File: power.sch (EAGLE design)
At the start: 19 parts, among them Q1 12V/6A, U1 LTC4412HV, X1 5566-4-RIGHTANGLE, X3 RASPI_BOARD_B+#_H

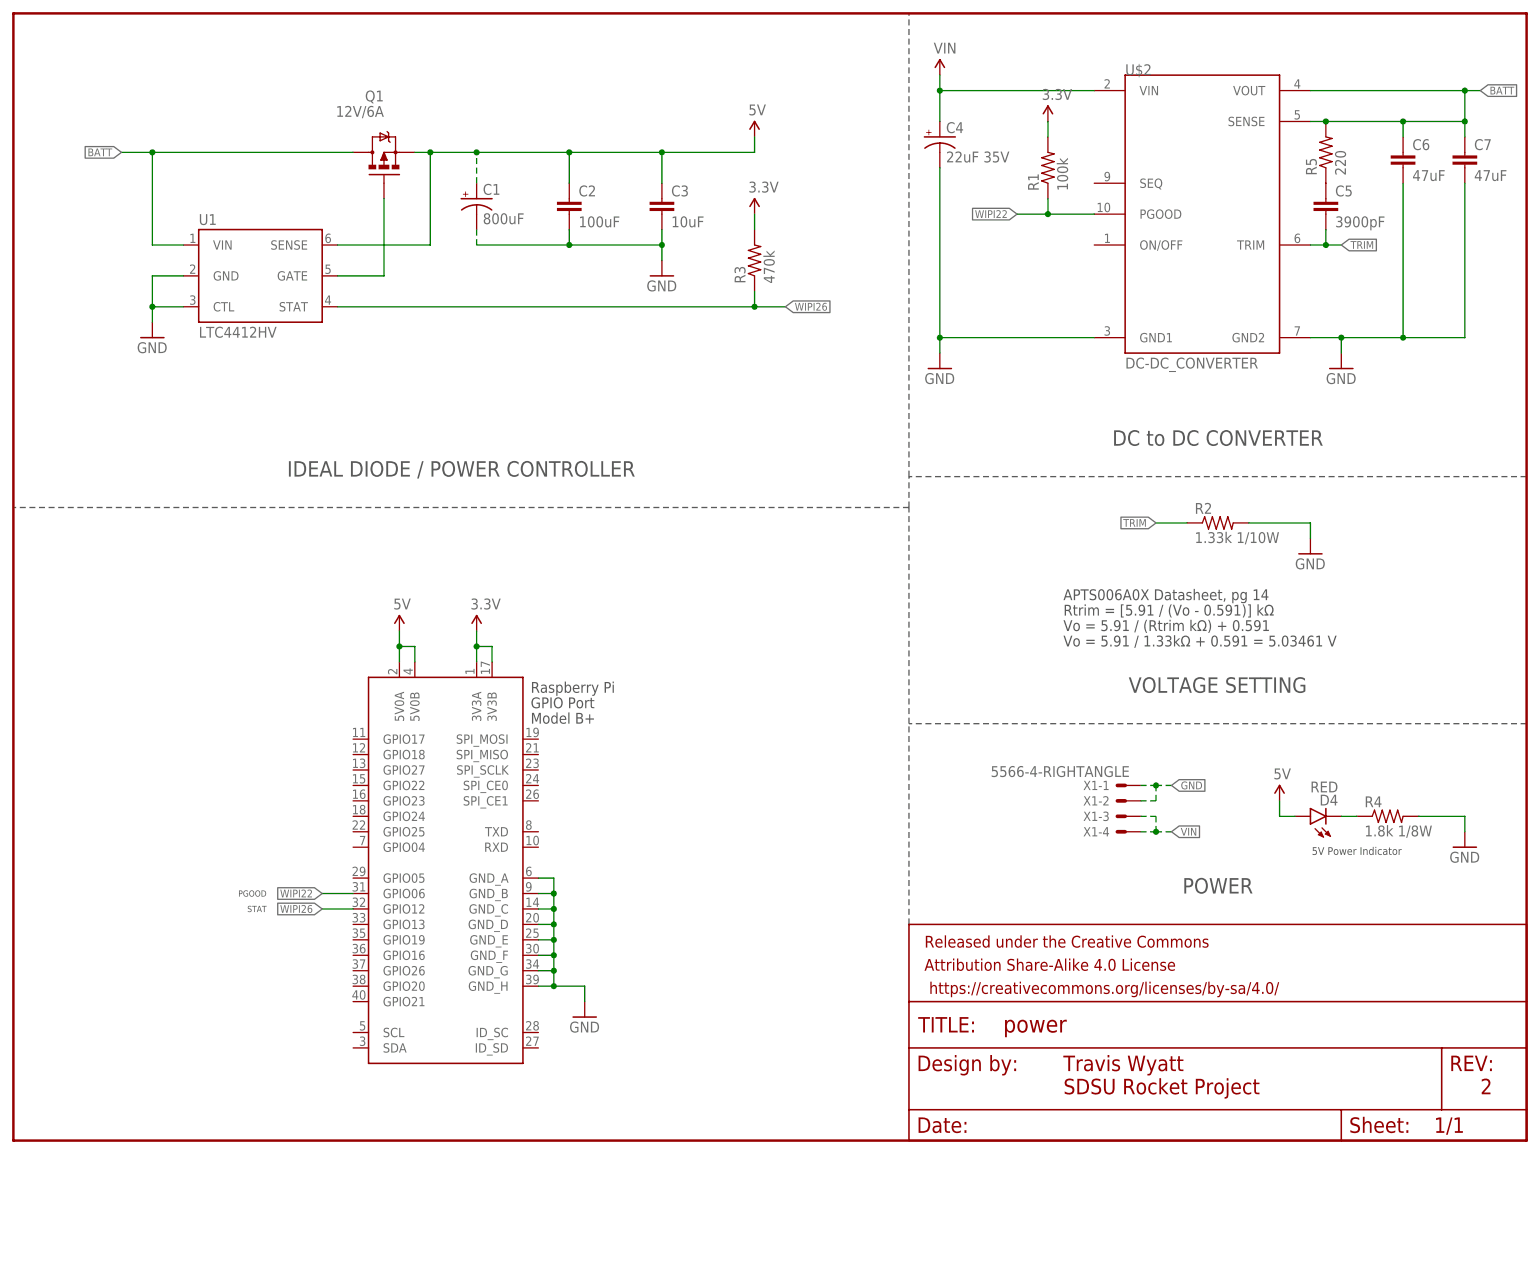
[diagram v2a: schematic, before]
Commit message: Optimize design and add voltage tuning
Updated design for more capacitor reuse and added additional capacitors
to help stabilize power. Added variable resistor to allow for fine
tuning voltage output. Improved labeling of components on the schematic.
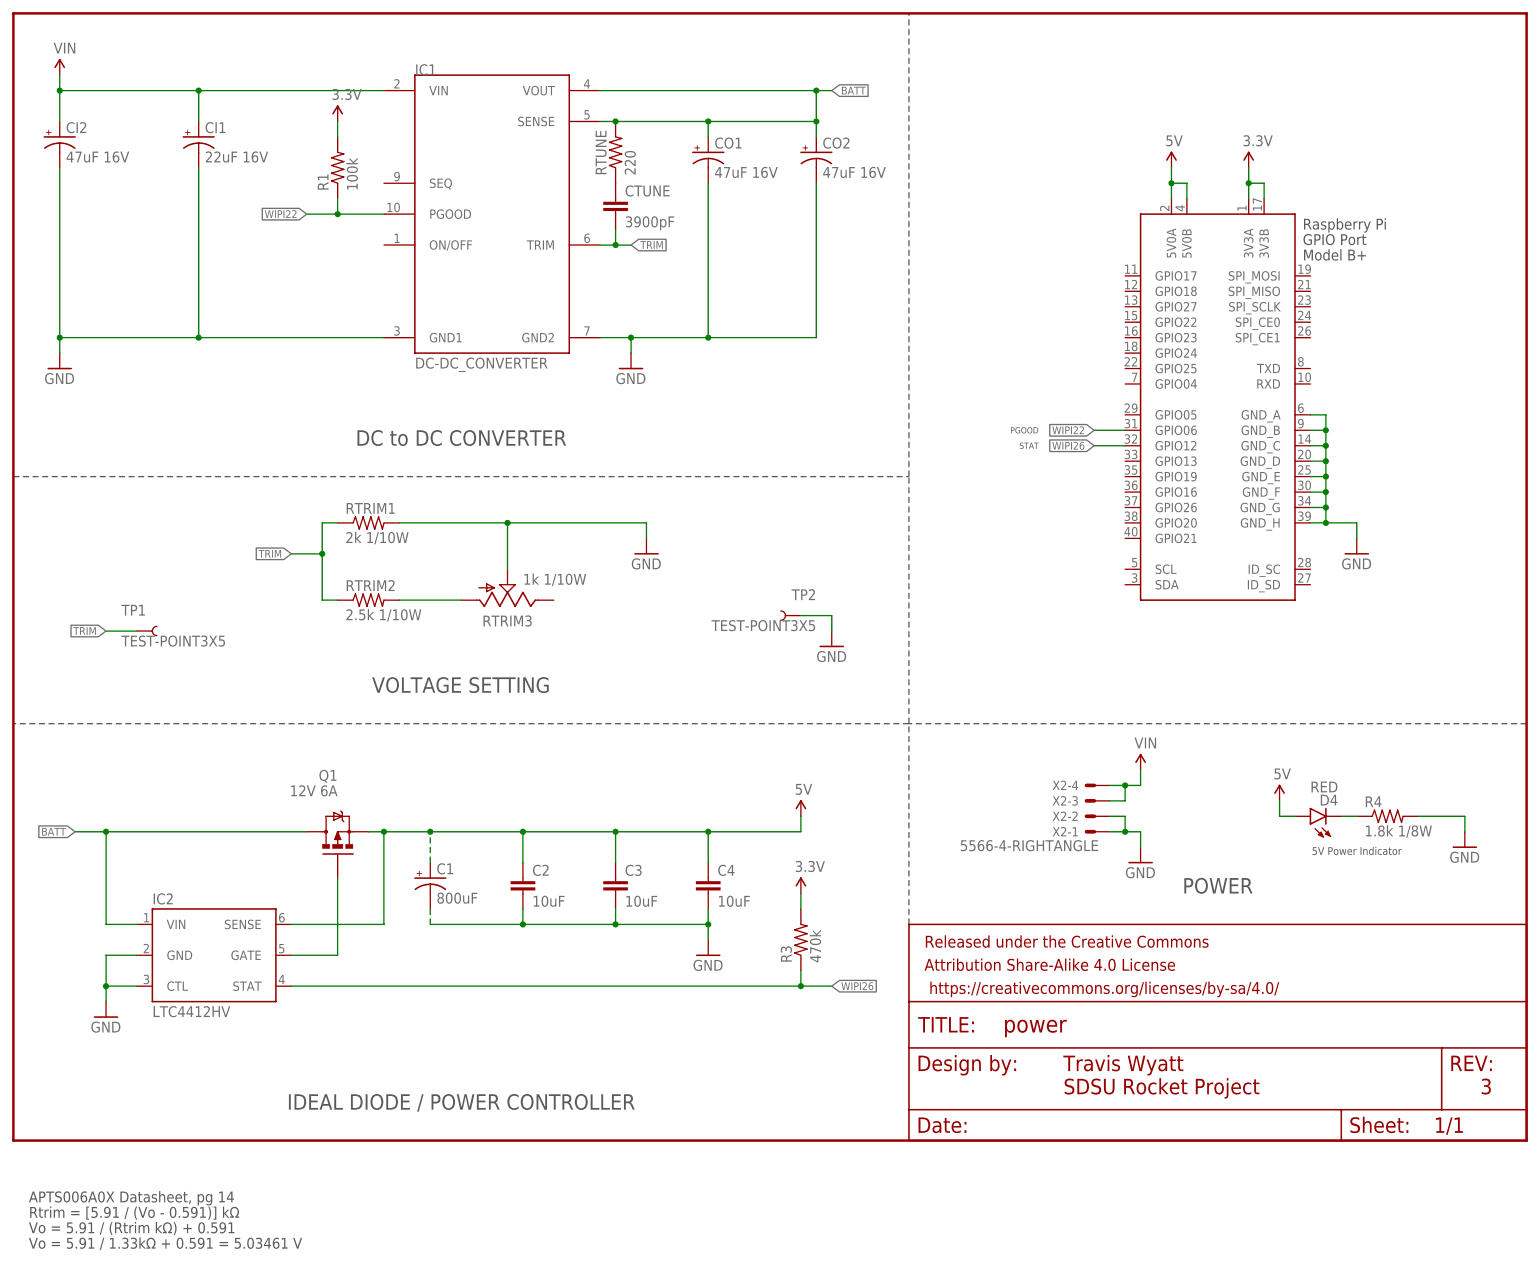
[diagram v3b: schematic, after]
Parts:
- removed C5: 3900pF, SparkFun-Capacitors:CAP0603-CAP
- removed C6, C7: 47uF, SparkFun-Capacitors:CAP0603-CAP
- removed R2: 1.33k 1/10W, SparkFun-Resistors:RESISTOR0603-RES
- removed R5: 220, SparkFun-Passives:RESISTOR0603-RES
- removed U$2: DC-DC_CONVERTER, SparkFun-PowerIC:DC-DC_CONVERTER
- removed U1: LTC4412HV, SDSURocket-PowerIC:LTC4412HV-SOT-23
- removed X1: 5566-4-RIGHTANGLE, SDSURocket-BreakoutBoards:5566-4-RIGHTANGLE
- added CI1: 22uF 16V, SparkFun-Capacitors:CAP_POLF80
- added CI2, CO1, CO2: 47uF 16V, SparkFun-Capacitors:CAP_POLF80
- added CTUNE: 3900pF, SparkFun-Capacitors:CAP0603-CAP
- added IC1: DC-DC_CONVERTER, SparkFun-PowerIC:DC-DC_CONVERTER
- added IC2: LTC4412HV, SDSURocket-PowerIC:LTC4412HV-SOT-23
- added RTRIM1: 2k 1/10W, SparkFun-Resistors:RESISTOR0603-RES
- added RTRIM2: 2.5k 1/10W, SparkFun-Resistors:RESISTOR0603-RES
- added RTRIM3: 1k 1/10W, SDSURocket-Electromechanical:POT-89P
- added RTUNE: 220, SparkFun-Passives:RESISTOR0603-RES
- added TP1, TP2: TEST-POINT3X5, SparkFun-Passives:TEST-POINT3X5
- added X2: 5566-4-RIGHTANGLE, SDSURocket-Connectors:5566-4-RIGHTANGLE
- C2: value 100uF -> 10uF
- C4: value 22uF 35V -> 10uF; device SparkFun-Capacitors:CAP_POLC -> SparkFun-Capacitors:CAP0603-CAP
- Q1: value 12V/6A -> 12V 6A
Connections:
- new net N$3: RTRIM2.2, RTRIM3.A
- net 5V: now also C4.1, IC2.SENSE; no longer U1.SENSE
- net BATT: now also CO1.+, CO2.+, IC1.SENSE, IC1.VOUT, IC2.VIN, RTUNE.2; no longer C6.1, C7.1, R5.2, U$2.SENSE, U$2.VOUT, U1.VIN
- net GND: now also C4.2, CI1.-, CI2.-, CO1.-, CO2.-, IC1.GND1, IC1.GND2, IC2.CTL, IC2.GND, RTRIM1.2, RTRIM3.S, TP2.1, X2-1.S, X2-2.S; no longer C4.-, C6.2, C7.2, R2.2, U$2.GND1, U$2.GND2, U1.CTL, U1.GND, X1-1.S, X1-2.S
- net N$1: now also IC2.GATE; no longer U1.GATE
- net N$2: now also CTUNE.1, RTUNE.1; no longer C5.1, R5.1
- net TRIM: now also CTUNE.2, IC1.TRIM, RTRIM1.1, RTRIM2.1, TP1.1; no longer C5.2, R2.1, U$2.TRIM
- net VIN: now also CI1.+, CI2.+, IC1.VIN, X2-3.S, X2-4.S; no longer C4.+, U$2.VIN, X1-3.S, X1-4.S
- net WIPI22: now also IC1.PGOOD; no longer U$2.PGOOD
- net WIPI26: now also IC2.STAT; no longer U1.STAT
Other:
- note added: "3"
- note removed: "2"
- moved on the sheet: C1, C2, C3, Q1, R1, R3

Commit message: Fix variable resistor thru holes
The thru hole positions and size for the variable resistor (RTRIM3) were
fixed to have the component sit on the top side of the board.
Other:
- note added: "4"
- note removed: "3"
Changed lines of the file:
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@@
 <text x="220.98" y="48.26" size="1.27" layer="97" align="top-center">5V Power Indicator</text>
 <text x="198.12" y="40.64" size="2.54" layer="97" align="bottom-center">POWER</text>
-<text x="241.3" y="7.62" size="2.54" layer="94">3</text>
+<text x="241.3" y="7.62" size="2.54" layer="94">4</text>
 <text x="172.72" y="12.7" size="2.54" layer="94" align="center-left">Travis Wyatt</text>
 <text x="172.72" y="8.89" size="2.54" layer="94" align="center-left">SDSU Rocket Project</text>
